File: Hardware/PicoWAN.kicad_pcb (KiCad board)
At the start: 2 copper layers, 50.8 x 22.9 mm, 55 parts, among them J1 Battery, J2 SWD, J3 Conn_left, J4 Conn_right, P1 USB_C_Plug_USB2.0, Q1 DMG3415U-7, U1 AP2112K-3.3, U2 RP2040, U3 MCP73831-2-OT, U4 W25Q16JV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

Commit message: update crystal and traces
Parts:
- removed Y1: 12Mhz, Crystal:Crystal_SMD_2520-4Pin_2.5x2.0mm
- added Y2: 12Mhz, Crystal:Crystal_SMD_2520-4Pin_2.5x2.0mm, F.Cu at (153.2, 87.1)
- renumbered BOOT to SW1, RST to SW2
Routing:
- net /EN: track 15.9 -> 21.4 mm
- net GND: track 133.3 -> 135.9 mm
- net Net-(C2-Pad1): track 8.07 -> 6.13 mm
- net Net-(C1-Pad1): track 8.57 -> 7.86 mm
- net /RX: track 25.1 -> 24.5 mm

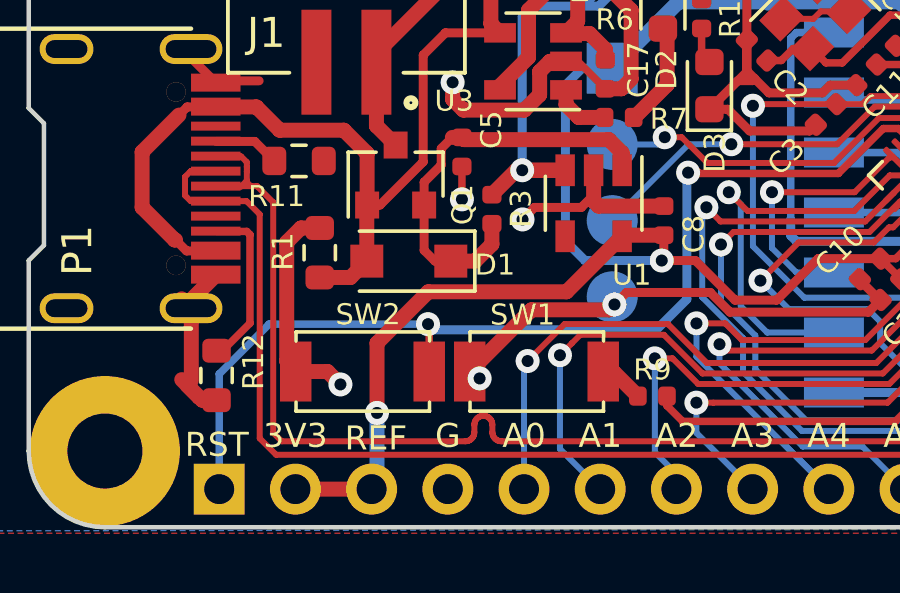
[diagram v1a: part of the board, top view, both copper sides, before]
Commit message: Add_Bat conector_BOM
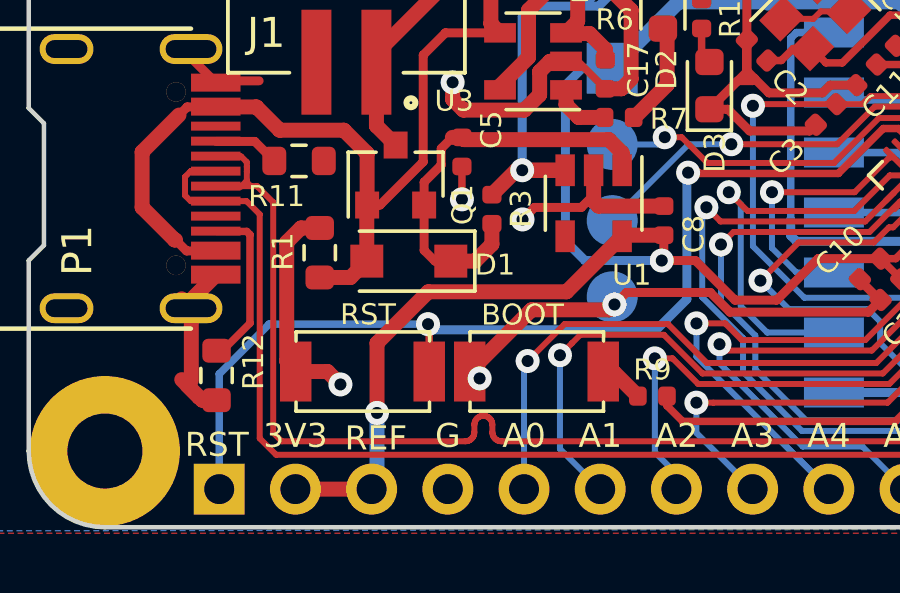
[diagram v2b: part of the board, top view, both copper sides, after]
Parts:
- renumbered SW1 to BOOT, SW2 to RST

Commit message: nRouteinProgress
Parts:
- removed BOOT: BOOT, Connectors:C455281
- added SW1: BOOT, KiCadLibraries:TS1088R02026, F.Cu at (143.8, 99.1)
- D2: value LED -> BAT
- SW2: renamed from RST; footprint Connectors:C455281 -> KiCadLibraries:TS1088R02026
- moved SW2 3.35 mm to (138.0, 99.1)
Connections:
- U2 pad 16: /D12 -> /CIPO_1
- U2 pad 17: /D13 -> /SCK_1
- U2 pad 18: /SCK_1 -> /COPI_1
- U2 pad 27: /CIPO_1 -> /CIPO_0
- U2 pad 28: /COPI_1 -> /CS_1
- U2 pad 31: /CIPO_0 -> /D12
- U2 pad 32: /CS_1 -> /D13
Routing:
- net /COPI_0: track 23.0 -> 0.00 mm, vias 1 -> 0
- net /SCK_0: track 22.5 -> 0.00 mm, vias 1 -> 0
- net /CIPO_0: track 22.4 -> 0.00 mm, vias 1 -> 0
- net /CIPO_1: track 15.1 -> 0.00 mm, vias 1 -> 0
- net /D13: track 16.5 -> 4.67 mm
- net /D12: track 9.37 -> 0.00 mm
- net /COPI_1: track 8.80 -> 0.00 mm, vias 1 -> 0
- net GND: track 135.9 -> 138.8 mm
- net /CS_1: track 5.16 -> 2.47 mm

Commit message: RoutedPCB
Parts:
- moved R2 0.12 mm to (156.3, 87.7)
- moved C11 0.07 mm to (155.0, 89.0)
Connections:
- J3 pad 11: /SCK_0 -> /CIPO_0
- J3 pad 12: /COPI_0 -> /SCK_0
- J3 pad 13: /CIPO_0 -> /COPI_0
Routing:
- net /COPI_0: track 0.00 -> 23.7 mm, vias 0 -> 1
- net /SCK_0: track 0.00 -> 22.5 mm, vias 0 -> 1
- net /CIPO_0: track 0.00 -> 22.5 mm, vias 0 -> 1
- net /D12: track 0.00 -> 21.5 mm, vias 0 -> 2
- net /D13: track 4.67 -> 22.7 mm, vias 0 -> 2
- net GND: track 138.8 -> 156.7 mm
- net /CIPO_1: track 0.00 -> 12.1 mm, vias 0 -> 1
- net /COPI_1: track 0.00 -> 9.43 mm, vias 0 -> 1
- net +1V2: track 29.9 -> 32.2 mm
- net /DIO5: track 15.4 -> 13.1 mm
- net /D24: track 19.6 -> 17.7 mm
- net +3V3: track 129.5 -> 128.0 mm
- net /DIO1: track 13.7 -> 12.4 mm
- net /DIO0: track 13.8 -> 12.5 mm
- net /RST: track 34.9 -> 33.8 mm
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
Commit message: Correction_Tracks
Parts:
- moved C9 1.51 mm to (158.4, 98.1), turned to 225 degrees
- moved R5 0.95 mm to (161.2, 98.8)
- moved C4 0.84 mm to (159.1, 98.8), turned to 225 degrees
- moved R9 0.77 mm to (148.5, 100.0)
- moved SW1 0.46 mm to (144.3, 99.1)
- moved R4 0.45 mm to (162.3, 99.1)
- moved SW2 0.36 mm to (138.4, 99.1)
- moved C11 0.31 mm to (155.2, 88.8)
- moved R2 0.28 mm to (156.5, 87.4), turned to 45 degrees
- moved C6 0.23 mm to (163.9, 96.3)
- moved C19 0.18 mm to (166.3, 97.7)
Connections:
- net Net-(R4-Pad2) renamed /RD+
- net Net-(R5-Pad2) renamed /RD-
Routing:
- net /EN: track 21.4 -> 15.0 mm
- net /D-: track 43.1 -> 41.0 mm
- net /D+: track 41.3 -> 39.6 mm
- net /RD-: track 1.89 -> 3.39 mm
- net /D11: track 6.96 -> 8.37 mm
- net /D13: track 22.7 -> 21.4 mm
- net /QSPI_CS: track 32.2 -> 30.9 mm
- net GND: track 156.7 -> 155.5 mm, vias 36 -> 42
- net /COPI_0: track 23.7 -> 24.6 mm
- net Net-(C2-Pad1): track 6.37 -> 5.44 mm
- net /DIO1: track 12.4 -> 13.2 mm
- net /SCK_0: track 22.5 -> 23.3 mm
- net /A3: track 15.1 -> 14.4 mm
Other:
- rule via_min_size: 0.4 -> 0.3

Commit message: Update_kicad_6
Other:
- net class Default removed
- net class Source removed
- net class VCC removed
